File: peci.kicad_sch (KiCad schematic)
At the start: 21 parts, among them Q1 PJE138K, U17 TXS0102DQER, U18 MAX6621AUB

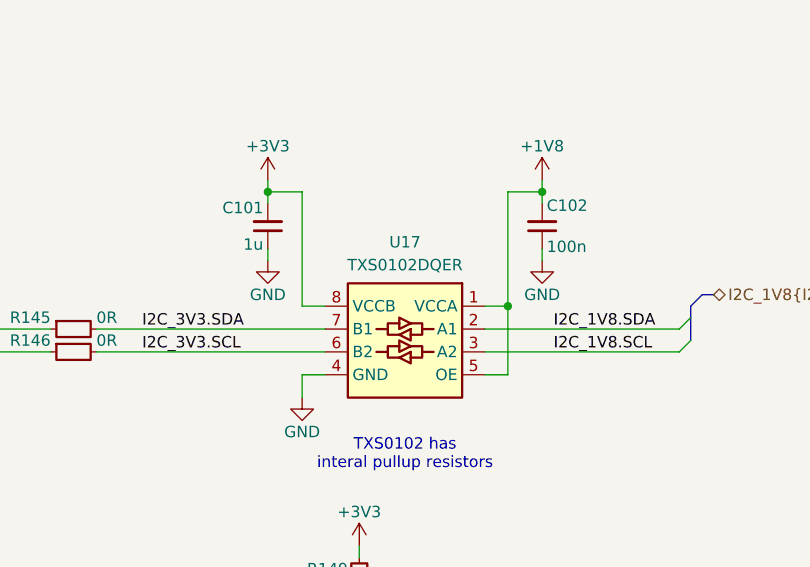
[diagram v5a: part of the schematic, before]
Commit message: [#100595] Update connections according to client request
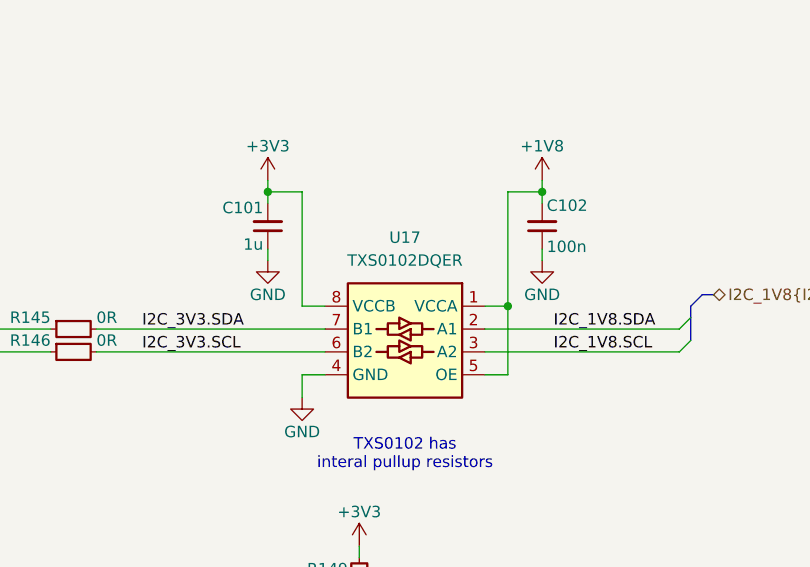
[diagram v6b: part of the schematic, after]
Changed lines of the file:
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@@
+	)
+	(symbol
+		(lib_id "antmicroLogicTranslatorsLevelShifters:TXS0102DQER")
+		(at 264.16 137.16 0)
+		(mirror y)
+		(unit 1)
+		(body_style 1)
+		(exclude_from_sim no)
+		(in_bom yes)
+		(on_board yes)
+		(in_pos_files yes)
+		(dnp no)
+		(fields_autoplaced yes)
+		(property "Reference" "U17"
+			(at 255.27 129.54 0)
+			(show_name no)
+			(do_not_autoplace no)
+			(effects
+				(font
+					(size 1.27 1.27)
+					(thickness 0.15)
+				)
+			)
+		)
+		(property "Value" "TXS0102DQER"
+			(at 231.14 144.78 0)
+			(hide yes)
+			(show_name no)
+			(do_not_autoplace no)
+			(effects
+				(font
+					(size 1.27 1.27)
+					(thickness 0.15)
+				)
+				(justify left bottom)
+			)
+		)
+		(property "Footprint" "antmicro-footprints:X2SON8_1.4x1x0.32mm_P0.35mm"
+			(at 231.14 147.32 0)
+			(hide yes)
+			(show_name no)
+			(do_not_autoplace no)
+			(effects
+				(font
+					(size 1.27 1.27)
+					(thickness 0.15)
+				)
+				(justify left bottom)
+			)
+		)
+		(property "Datasheet" "https://www.ti.com/lit/ds/symlink/txs0102.pdf?ts=1637914596981&ref_url=https%253A%252F%252Fwww.ti.com%252Fstore%252Fti%252Fen%252Fp%252Fproduct%252F%253Fp%253DTXS0102DCTR%2526keyMatch%253DTXS0102DCTR%2526tisearch%253Dsearch-everything%2526usecase%253DOPN"
+			(at 231.14 149.86 0)
+			(hide yes)
+			(show_name no)
+			(do_not_autoplace no)
+			(effects
+				(font
+					(size 1.27 1.27)
+					(thickness 0.15)
+				)
+				(justify left bottom)
+			)
+		)
+		(property "Description" "Level shifter"
+			(at 231.14 162.56 0)
+			(hide yes)
+			(show_name no)
+			(do_not_autoplace no)
+			(effects
+				(font
+					(size 1.27 1.27)
+				)
+				(justify left bottom)
+			)
+		)
+		(property "MPN" "TXS0102DQER"
+			(at 255.27 132.08 0)
+			(show_name no)
+			(do_not_autoplace no)
+			(effects
+				(font
+					(size 1.27 1.27)
+					(thickness 0.15)
+				)
+			)
+		)
+		(property "Manufacturer" "Texas Instruments"
+			(at 231.14 154.94 0)
+			(hide yes)
+			(show_name no)
+			(do_not_autoplace no)
+			(effects
+				(font
+					(size 1.27 1.27)
+					(thickness 0.15)
+				)
+				(justify left bottom)
+			)
+		)
+		(property "Author" "Antmicro"
+			(at 231.14 157.48 0)
+			(hide yes)
+			(show_name no)
+			(do_not_autoplace no)
+			(effects
+				(font
+					(size 1.27 1.27)
+					(thickness 0.15)
+				)
+				(justify left bottom)
+			)
+		)
+		(property "License" "Apache-2.0"
+			(at 231.14 160.02 0)
+			(hide yes)
+			(show_name no)
+			(do_not_autoplace no)
+			(effects
+				(font
+					(size 1.27 1.27)
+					(thickness 0.15)
+				)
+				(justify left bottom)
+			)
+		)
+		(pin "8"
+		)
+		(pin "3"
+		)
+		(pin "2"
+		)
+		(pin "1"
+		)
+		(pin "5"
+		)
+		(pin "6"
+		)
+		(pin "4"
+		)
+		(pin "7"
+		)
+		(instances
+			(project "altera-modular-agilex-5-dc-scm"
+				(path "/6bb9d978-a328-4b30-874b-55170a976185/b18fedc8-291b-45fb-9413-07ab4e9140fd"
+					(reference "U17")
+					(unit 1)
+				)
+			)
+		)
 	)
 	(symbol
@@
 					(unit 1)
 				)
-			)
-		)
-	)
-	(symbol
-		(lib_id "antmicroLogicTranslatorsLevelShifters:TXS0102DQER")
-		(at 264.16 134.62 0)
-		(mirror y)
-		(unit 1)
-		(body_style 1)
-		(exclude_from_sim no)
-		(in_bom yes)
-		(on_board yes)
-		(in_pos_files yes)
-		(dnp no)
-		(property "Reference" "U17"
-			(at 255.27 130.048 0)
-			(show_name no)
-			(do_not_autoplace no)
-			(effects
-				(font
-					(size 1.27 1.27)
-					(thickness 0.15)
-				)
-			)
-		)
-		(property "Value" "TXS0102DQER"
-			(at 231.14 142.24 0)
-			(hide yes)
-			(show_name no)
-			(do_not_autoplace no)
-			(effects
-				(font
-					(size 1.27 1.27)
-					(thickness 0.15)
-				)
-				(justify left bottom)
-			)
-		)
-		(property "Footprint" "antmicro-footprints:X2SON8_1.4x1x0.32mm_P0.35mm"
-			(at 231.14 144.78 0)
-			(hide yes)
-			(show_name no)
-			(do_not_autoplace no)
-			(effects
-				(font
-					(size 1.27 1.27)
-					(thickness 0.15)
-				)
-				(justify left bottom)
-			)
-		)
-		(property "Datasheet" "https://www.ti.com/lit/ds/symlink/txs0102.pdf?ts=1637914596981&ref_url=https%253A%252F%252Fwww.ti.com%252Fstore%252Fti%252Fen%252Fp%252Fproduct%252F%253Fp%253DTXS0102DCTR%2526keyMatch%253DTXS0102DCTR%2526tisearch%253Dsearch-everything%2526usecase%253DOPN"
-			(at 231.14 147.32 0)
-			(hide yes)
-			(show_name no)
-			(do_not_autoplace no)
-			(effects
-				(font
-					(size 1.27 1.27)
-					(thickness 0.15)
-				)
-				(justify left bottom)
-			)
-		)
-		(property "Description" "Level shifter"
-			(at 231.14 160.02 0)
-			(hide yes)
-			(show_name no)
-			(do_not_autoplace no)
-			(effects
-				(font
-					(size 1.27 1.27)
-				)
-				(justify left bottom)
-			)
-		)
-		(property "MPN" "TXS0102DQER"
-			(at 255.27 132.588 0)
-			(show_name no)
-			(do_not_autoplace no)
-			(effects
-				(font
-					(size 1.27 1.27)
-					(thickness 0.15)
-				)
-			)
-		)
-		(property "Manufacturer" "Texas Instruments"
-			(at 231.14 152.4 0)
-			(hide yes)
-			(show_name no)
-			(do_not_autoplace no)
-			(effects
-				(font
-					(size 1.27 1.27)
-					(thickness 0.15)
-				)
-				(justify left bottom)
-			)
-		)
-		(property "Author" "Antmicro"
-			(at 231.14 154.94 0)
-			(hide yes)
-			(show_name no)
-			(do_not_autoplace no)
-			(effects
-				(font
-					(size 1.27 1.27)
-					(thickness 0.15)
-				)
-				(justify left bottom)
-			)
-		)
-		(property "License" "Apache-2.0"
-			(at 231.14 157.48 0)
-			(hide yes)
-			(show_name no)
-			(do_not_autoplace no)
-			(effects
-				(font
-					(size 1.27 1.27)
-					(thickness 0.15)
-				)
-				(justify left bottom)
-			)
-		)
-		(pin "8"
-		)
-		(pin "3"
-		)
-		(pin "2"
-		)
-		(pin "1"
-		)
-		(pin "5"
-		)
-		(pin "6"
-		)
-		(pin "4"
-		)
-		(pin "7"
-		)
-		(instances
-			(project "altera-modular-agilex-5-dc-scm"
-				(path "/6bb9d978-a328-4b30-874b-55170a976185/b18fedc8-291b-45fb-9413-07ab4e9140fd"
-					(reference "U17")
-					(unit 1)
-				)

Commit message: [#100501] Reannotate schematic
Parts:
- renumbered C101 to C105, C102 to C106, C103 to C107, C104 to C108, Q1 to Q3, R145 to R179, R146 to R180, R147 to R181, R148 to R182, R149 to R183, R150 to R184, R151 to R185, R152 to R186, TP14 to TP18, TP15 to TP19, TP16 to TP20, TP17 to TP21, TP18 to TP22, TP19 to TP23, U18 to U16

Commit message: [#100501] Perform minor BOM consolidation
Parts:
- C105: value C_1u_0402 -> C_1u_25V_0402; symbol antmicroCapacitors0402:C_1u_0402 -> antmicroCapacitors0402:C_1u_25V_0402; Dielectric (none) -> X5R; MPN C1005X6S1A105K050BC -> GRM155R61E105KE11J; Manufacturer TDK -> Murata; Voltage (none) -> 25V
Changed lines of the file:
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@@
 	)
 	(symbol
-		(lib_id "antmicroCapacitors0402:C_1u_0402")
+		(lib_id "antmicroCapacitors0402:C_1u_25V_0402")
 		(at 240.03 130.81 270)
 		(mirror x)
@@
 			)
 		)
-		(property "Value" "C_1u_0402"
+		(property "Value" "C_1u_25V_0402"
 			(at 229.87 110.49 0)
 			(hide yes)
@@
 			)
 		)
-		(property "Datasheet" "https://product.tdk.com/en/search/capacitor/ceramic/mlcc/info?part_no=C1005X6S1A105K050BC"
+		(property "Datasheet" "https://www.murata.com/products/productdetail?partno=GRM155R61E105KE11%23"
 			(at 224.79 110.49 0)
 			(hide yes)
@@
 			)
 		)
-		(property "Description" "SMD Multilayer Ceramic Capacitor, 1 µF, 10 V, 0402 [1005 Metric], ± 10%, X6S, C"
+		(property "Description" "SMD Multilayer Ceramic Capacitor, 1 µF, 25 V, 0402 [1005 Metric], ± 10%, X5R, GRM Series"
 			(at 207.01 110.49 0)
 			(hide yes)
@@
 			)
 		)
-		(property "MPN" "C1005X6S1A105K050BC"
+		(property "MPN" "GRM155R61E105KE11J"
 			(at 222.25 110.49 0)
 			(hide yes)
@@
 			)
 		)
-		(property "Manufacturer" "TDK"
+		(property "Manufacturer" "Murata"
 			(at 219.71 110.49 0)
 			(hide yes)
@@
 			)
 		)
-		(property "Voltage" ""
+		(property "Voltage" "25V"
 			(at 212.09 110.49 0)
 			(hide yes)
@@
 			)
 		)
-		(property "Dielectric" ""
+		(property "Dielectric" "X5R"
 			(at 209.55 110.49 0)
 			(hide yes)
